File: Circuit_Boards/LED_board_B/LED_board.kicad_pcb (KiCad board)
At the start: 2 copper layers, 39 x 39 mm, 12 parts, among them J1 Conn_01x03, U1 IS32LT3954

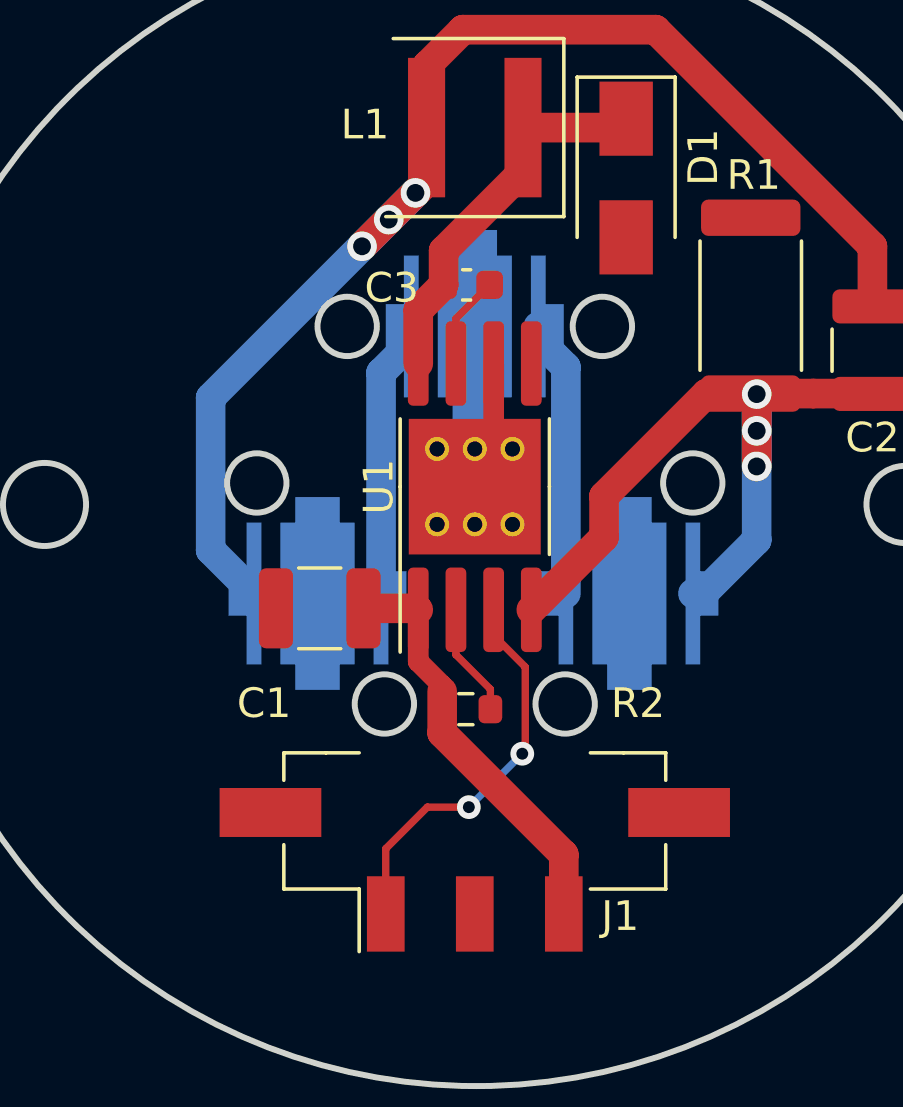
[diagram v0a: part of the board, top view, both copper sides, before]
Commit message: removed BOM and gerbers for kicad project, to ensure up to date exports
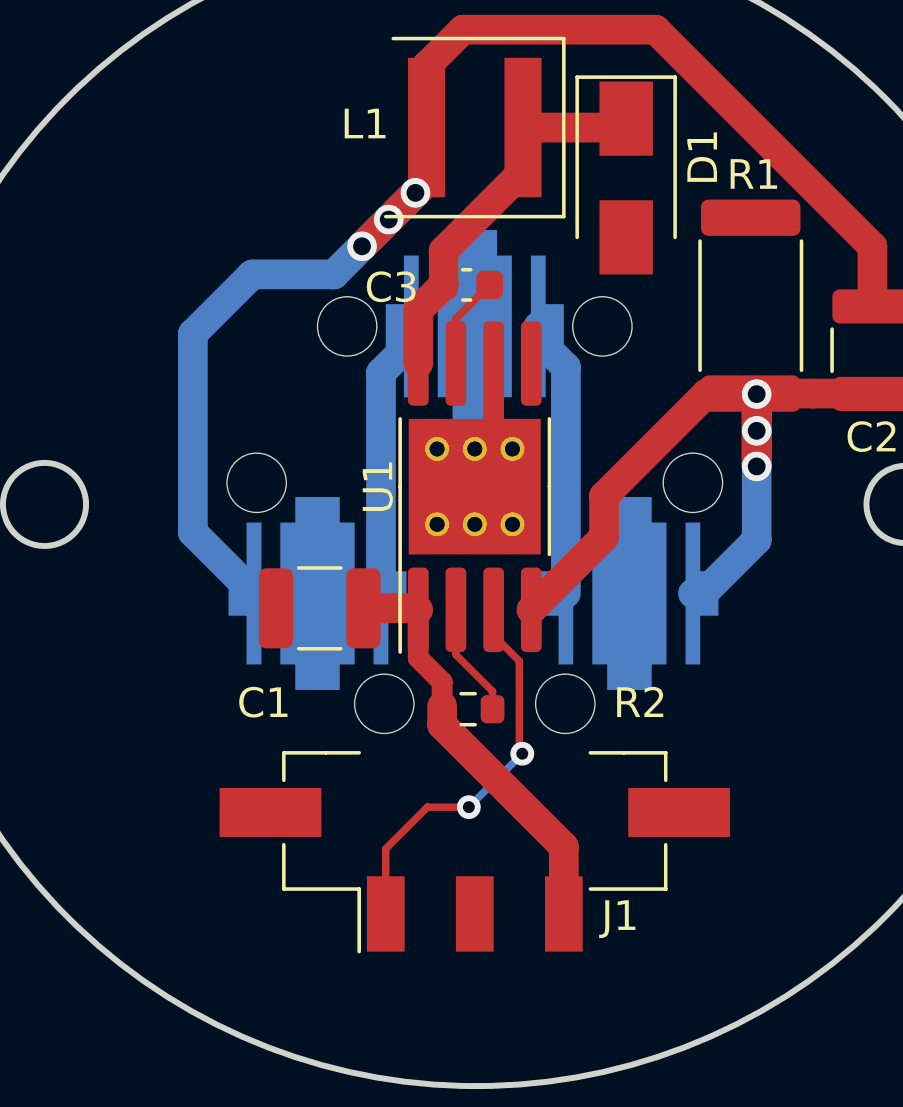
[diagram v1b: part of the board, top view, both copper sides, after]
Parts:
- added M1: Lens_Mount, CustomLibrary:LEDiL_Clip, B.Cu at (116.0, 102.9)
- added M2: Lens_Mount, CustomLibrary:LEDiL_Clip, B.Cu at (121.2, 93.9)
- added M3: Lens_Mount, CustomLibrary:LEDiL_Clip, B.Cu at (126.4, 102.9)
- R2: value 1K -> 1M
- moved R2 0.07 mm to (121.0, 106.8)
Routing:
- net /anode: track 42.7 -> 44.8 mm
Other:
- outline, holes or cut-outs redrawn
